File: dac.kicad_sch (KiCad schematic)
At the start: 27 parts, among them U13 L78L05_SOT89, U14 AK4454

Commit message: work on bugs
* align parts
* enlarge cercaps
* fix ak caps
* improve jack footprint
* fix lmr stencil openings
* remove one ldo
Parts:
- C105, C110: footprint invendelirium_general:CP_Radial_D8.0mm_P3.50mm -> invendelirium_general:CP_Radial_D6.3mm_P2.50mm
- C107, C108, C109, CU14: footprint invendelirium_audio:C_0603 -> invendelirium_audio:C_0603_larger
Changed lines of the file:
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@@
 			)
 		)
-		(property "Footprint" "invendelirium_audio:C_0603"
+		(property "Footprint" "invendelirium_audio:C_0603_larger"
 			(at 139.3952 45.72 0)
 			(effects
@@
 			)
 		)
-		(property "Footprint" "invendelirium_audio:C_0603"
+		(property "Footprint" "invendelirium_audio:C_0603_larger"
 			(at 148.2852 53.34 0)
 			(effects
@@
 			)
 		)
-		(property "Footprint" "invendelirium_general:CP_Radial_D8.0mm_P3.50mm"
+		(property "Footprint" "invendelirium_general:CP_Radial_D6.3mm_P2.50mm"
 			(at 171.45 113.03 0)
 			(effects
@@
 			)
 		)
-		(property "Footprint" "invendelirium_audio:C_0603"
+		(property "Footprint" "invendelirium_audio:C_0603_larger"
 			(at 164.7952 118.11 0)
 			(effects
@@
 			)
 		)
-		(property "Footprint" "invendelirium_audio:C_0603"
+		(property "Footprint" "invendelirium_audio:C_0603_larger"
 			(at 129.2352 53.34 0)
 			(effects
@@
 			)
 		)
-		(property "Footprint" "invendelirium_general:CP_Radial_D8.0mm_P3.50mm"
+		(property "Footprint" "invendelirium_general:CP_Radial_D6.3mm_P2.50mm"
 			(at 127 30.48 0)
 			(effects

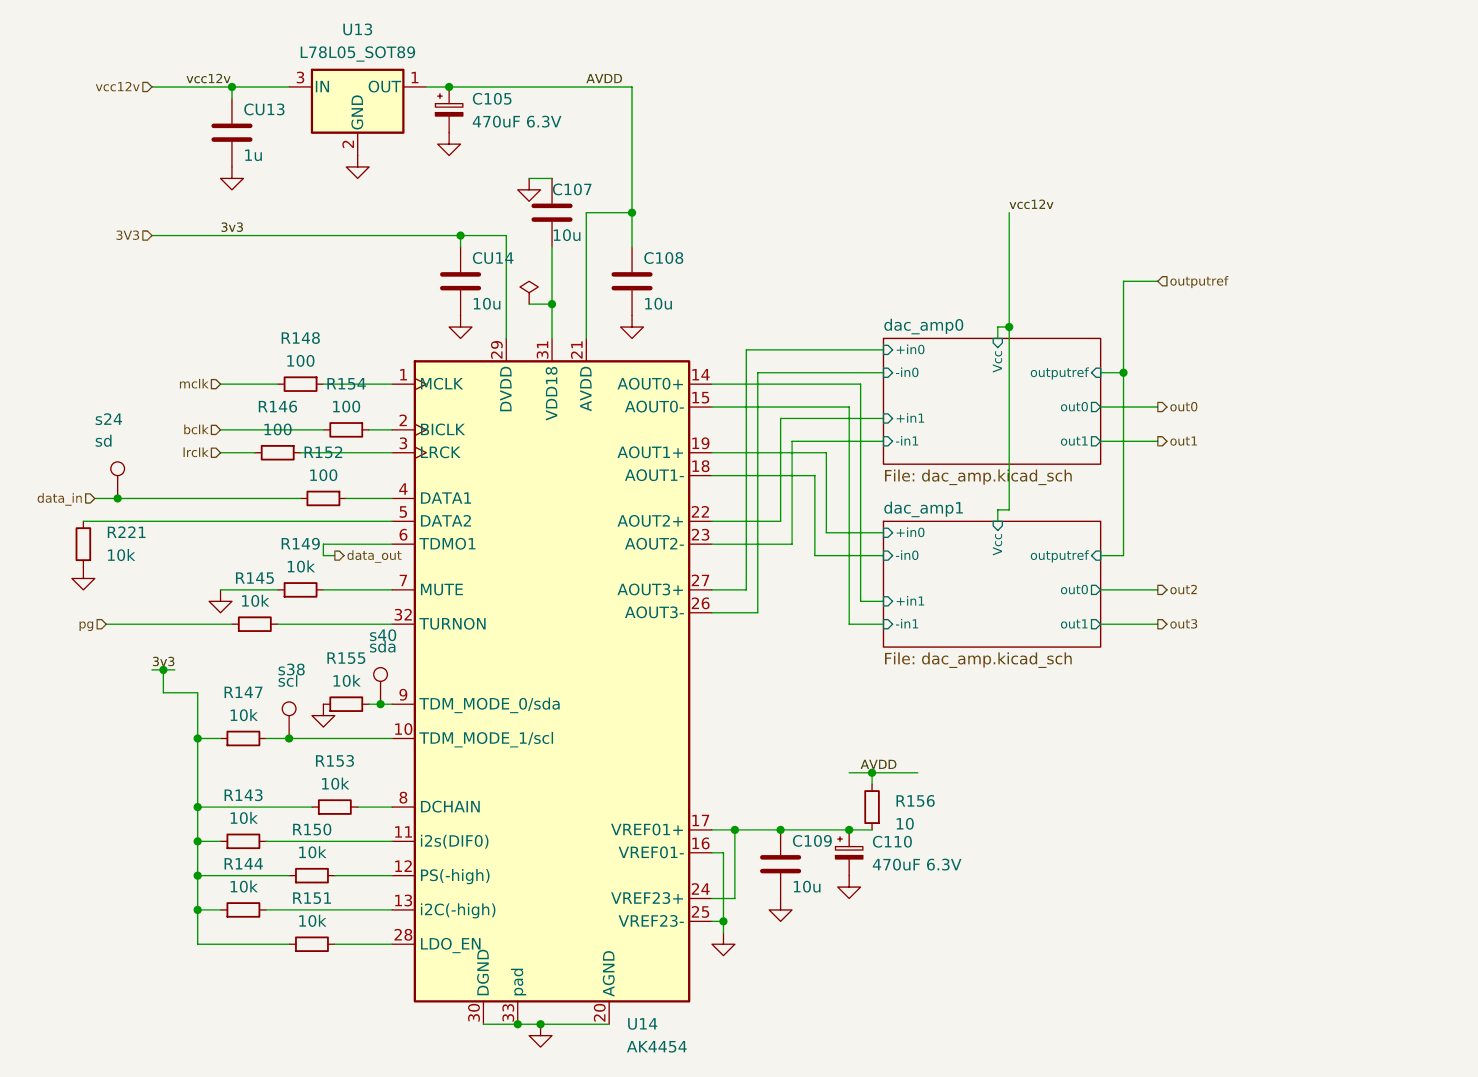
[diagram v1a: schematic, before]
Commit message: remove duplicate dac supply
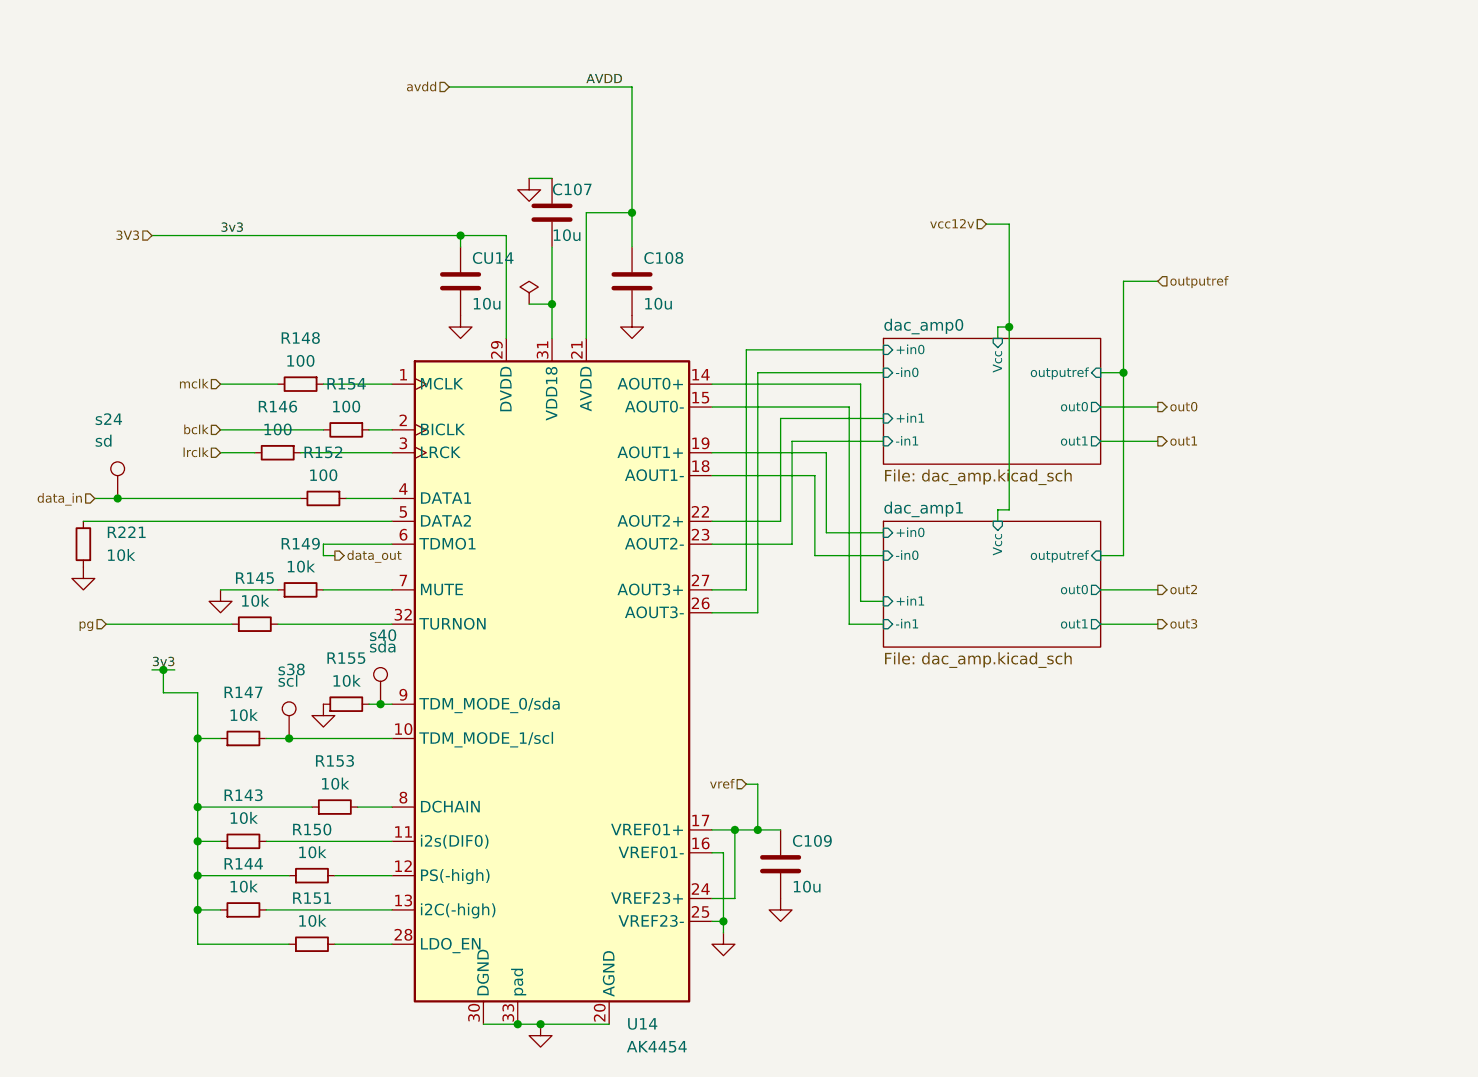
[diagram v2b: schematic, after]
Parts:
- removed C105, C110: 470uF 6.3V, invendelirium_general:CP_Radial_D6.3mm_P2.50mm, symbol Device:C_Polarized_Small
- removed CU13: 1u, invendelirium_audio:C_0603, symbol Device:C
- removed R156: 10, invendelirium_audio:R_0603, symbol Device:R_Small
- removed U13: L78L05_SOT89, Package_TO_SOT_SMD:SOT-89-3, symbol Regulator_Linear:L78L05_SOT89
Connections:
- net vref: now reaches C109.1, U14.17 (VREF01+), U14.24 (VREF23+)
- net AVDD renamed avdd

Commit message: all known bugs fixed
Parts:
- added s51: out0, invendelirium_general:pad_1.2x1.5, symbol Connector:TestPoint
- added s53: out1, invendelirium_general:pad_1.2x1.5, symbol Connector:TestPoint
- added s55: out2, invendelirium_general:pad_1.2x1.5, symbol Connector:TestPoint
- added s57: out3, invendelirium_general:pad_1.2x1.5, symbol Connector:TestPoint
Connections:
- net out0: now also s51.1
- net out1: now also s53.1
- net out2: now also s55.1
- net out3: now also s57.1

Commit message: rename testpoints?
i don't think it was intentional...
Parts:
- renumbered s51 to s52, s53 to s54, s55 to s56, s57 to s58
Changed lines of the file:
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@@
 		(on_board yes)
 		(dnp no)
-		(property "Reference" "s53"
+		(property "Reference" "s54"
 			(at 210.82 50.8 0)
 			(effects
@@
 		(on_board yes)
 		(dnp no)
-		(property "Reference" "s51"
+		(property "Reference" "s52"
 			(at 205.74 50.8 0)
 			(effects
@@
 		(on_board yes)
 		(dnp no)
-		(property "Reference" "s55"
+		(property "Reference" "s56"
 			(at 205.74 73.66 0)
 			(effects
@@
 		(on_board yes)
 		(dnp no)
-		(property "Reference" "s57"
+		(property "Reference" "s58"
 			(at 210.82 73.66 0)
 			(effects
